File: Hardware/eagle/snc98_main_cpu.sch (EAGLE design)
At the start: 88 parts, among them IC1 MCP170333MB, M1 IRLML2244, M12 IRLML2244, M2 IRLML2244, M3 IRLML2244, T1 BCR135, T2 BCR135, T3 BCR185, U1 74HC4051_MUX, U2 DS18B20, U3 ATMEGA1284P-PU, U4 TLV70033 / TC1185, Y2 12MHz

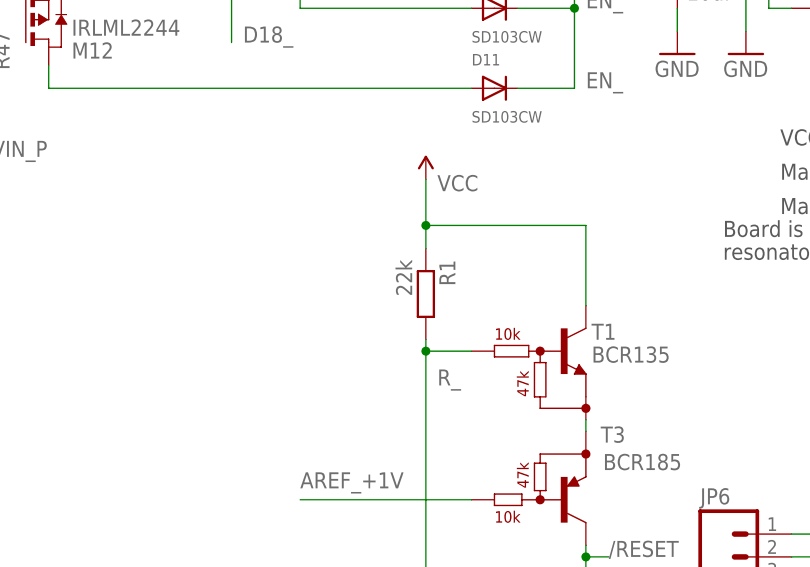
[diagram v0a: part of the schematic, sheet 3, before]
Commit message: Work like WIN_7 Calculator in "Standard Mode"
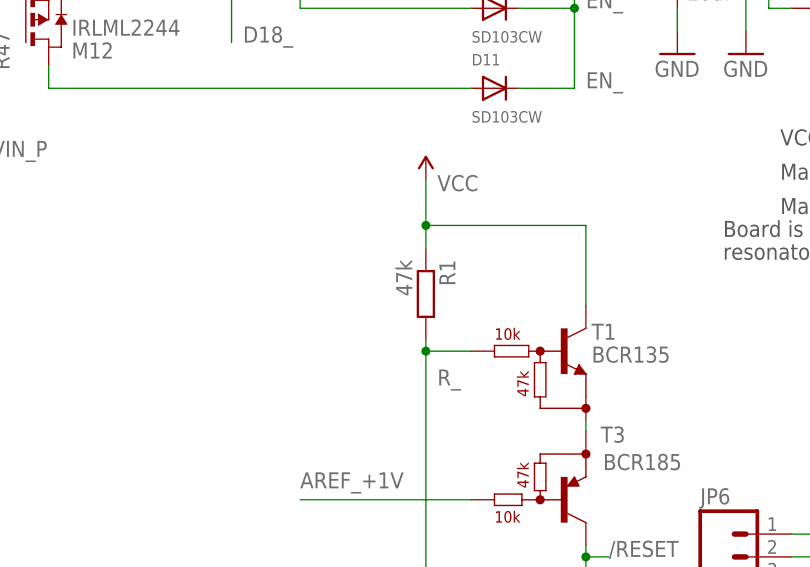
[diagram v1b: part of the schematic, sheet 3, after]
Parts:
- R1: value 22k -> 47k
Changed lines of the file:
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@@
 <setting verticaltext="up"/>
 </settings>
-<grid distance="0.1" unitdist="inch" unit="inch" style="lines" multiple="1" display="yes" altdistance="0.05" altunitdist="inch" altunit="inch"/>
+<grid distance="0.1" unitdist="inch" unit="mil" style="lines" multiple="1" display="no" altdistance="0.05" altunitdist="inch" altunit="inch"/>
 <layers>
 <layer number="1" name="Top" color="4" fill="1" visible="no" active="no"/>
@@
 <part name="U3" library="Atmel_By_element14_Batch_1-00" deviceset="ATMEGA1284P-PU" device=""/>
 <part name="R50" library="rcl" deviceset="R-EU_" device="R1206" value="6k8"/>
-<part name="R1" library="rcl" deviceset="R-EU_" device="R1206" value="22k"/>
+<part name="R1" library="rcl" deviceset="R-EU_" device="R1206" value="47k"/>
 <part name="R4" library="rcl" deviceset="R-EU_" device="R1206" value="100"/>
 <part name="R51" library="rcl" deviceset="R-EU_" device="R1206" value="3k3"/>

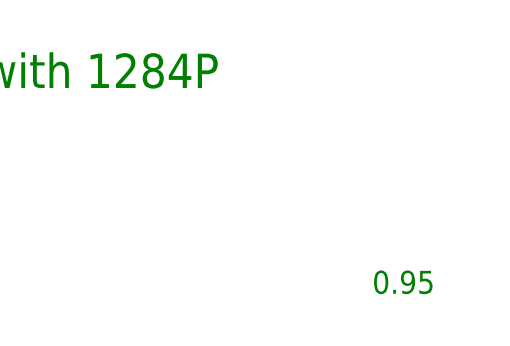
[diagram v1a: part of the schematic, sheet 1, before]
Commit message: Version 4 mechanical change
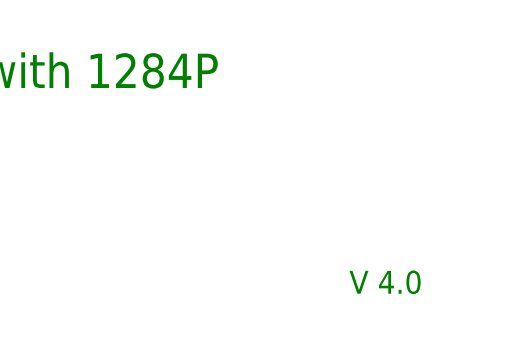
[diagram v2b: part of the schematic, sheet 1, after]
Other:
- note added: "V 4.0"
- note removed: "0.95"
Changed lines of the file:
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@@
 <setting verticaltext="up"/>
 </settings>
-<grid distance="0.1" unitdist="inch" unit="mil" style="lines" multiple="1" display="no" altdistance="0.05" altunitdist="inch" altunit="inch"/>
+<grid distance="0.1" unitdist="inch" unit="inch" style="lines" multiple="1" display="yes" altdistance="0.05" altunitdist="inch" altunit="inch"/>
 <layers>
 <layer number="1" name="Top" color="4" fill="1" visible="no" active="no"/>
@@
 <text x="149.86" y="30.48" size="3.81" layer="91" ratio="12">Calculator 15-Digit with 1284P</text>
 <text x="149.86" y="25.4" size="2.54" layer="91" ratio="12">by Jens Grabner</text>
-<text x="238.76" y="7.62" size="2.54" layer="91" ratio="12">0.95</text>
+<text x="236.22" y="7.62" size="2.54" layer="91" ratio="12">V 4.0</text>
 <text x="5.08" y="10.16" size="2.1844" layer="91" ratio="10">Calculator 15-Digit with ATmega1284P by Jens Grabner is licensed under</text>
 <text x="5.08" y="15.24" size="3.81" layer="91" ratio="12">Copyright CERN 2013</text>
@@
 <text x="149.86" y="30.48" size="3.81" layer="91" ratio="12">Calculator 15-Digit with 1284P</text>
 <text x="149.86" y="25.4" size="2.54" layer="91" ratio="12">by Jens Grabner</text>
-<text x="238.76" y="7.62" size="2.54" layer="91" ratio="12">0.95</text>
+<text x="236.22" y="7.62" size="2.54" layer="91" ratio="12">V 4.0</text>
 <text x="5.08" y="10.16" size="2.1844" layer="91" ratio="10">Calculator 15-Digit with ATmega1284P by Jens Grabner is licensed under</text>
 <text x="5.08" y="15.24" size="3.81" layer="91" ratio="12">Copyright CERN 2013</text>
@@
 <text x="149.86" y="30.48" size="3.81" layer="91" ratio="12">Calculator 15-Digit with 1284P</text>
 <text x="149.86" y="25.4" size="2.54" layer="91" ratio="12">by Jens Grabner</text>
-<text x="238.76" y="7.62" size="2.54" layer="91" ratio="12">0.95</text>
+<text x="236.22" y="7.62" size="2.54" layer="91" ratio="12">V 4.0</text>
 <text x="5.08" y="10.16" size="2.1844" layer="91" ratio="10">Calculator 15-Digit with ATmega1284P by Jens Grabner is licensed under</text>
 <text x="5.08" y="15.24" size="3.81" layer="91" ratio="12">Copyright CERN 2013</text>

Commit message: V 5.0 Hardware - Design
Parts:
- removed JP5: ICSP, _jc:AVR_SPI_PRG_62X3_LOCK
- added JP1: ICSP, _jc:AVR_SPI_PRG_6
- C12: value 47n -> 220n
- C2: value 100nF -> 220nF
- C20, C21: value 10uF -> 4.7uF
- C7, C8: value 22pF -> 15pF
- R25: value 1k -> 100
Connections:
- net /RESET: now also JP1.RST; no longer JP5.RST
- net D5_: now also JP1.MOSI; no longer JP5.MOSI
- net D6_: now also JP1.MISO; no longer JP5.MISO
- net D7_: now also JP1.SCK; no longer JP5.SCK
- net GND-ISO: now also JP1.GND; no longer JP5.GND
- net VCC: now also JP1.VCC; no longer JP5.VCC
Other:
- note added: "V 5.0"
- note removed: "V 4.0"

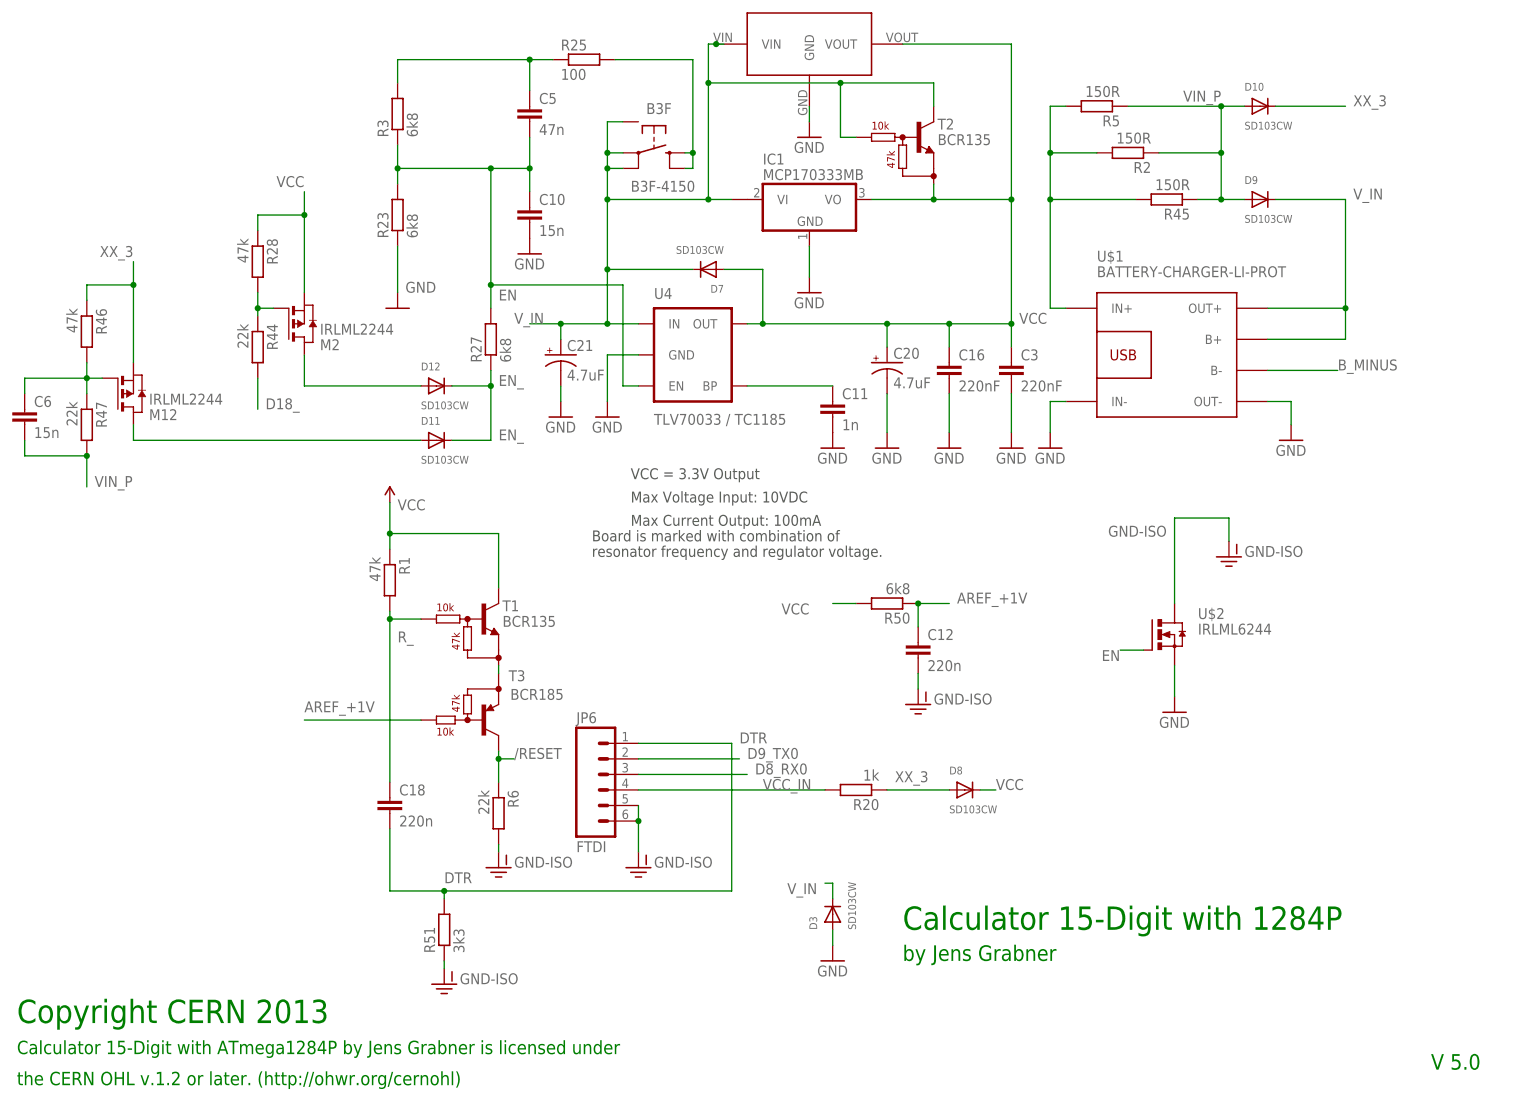
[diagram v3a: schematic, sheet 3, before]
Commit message: PCB cleaning V1.1
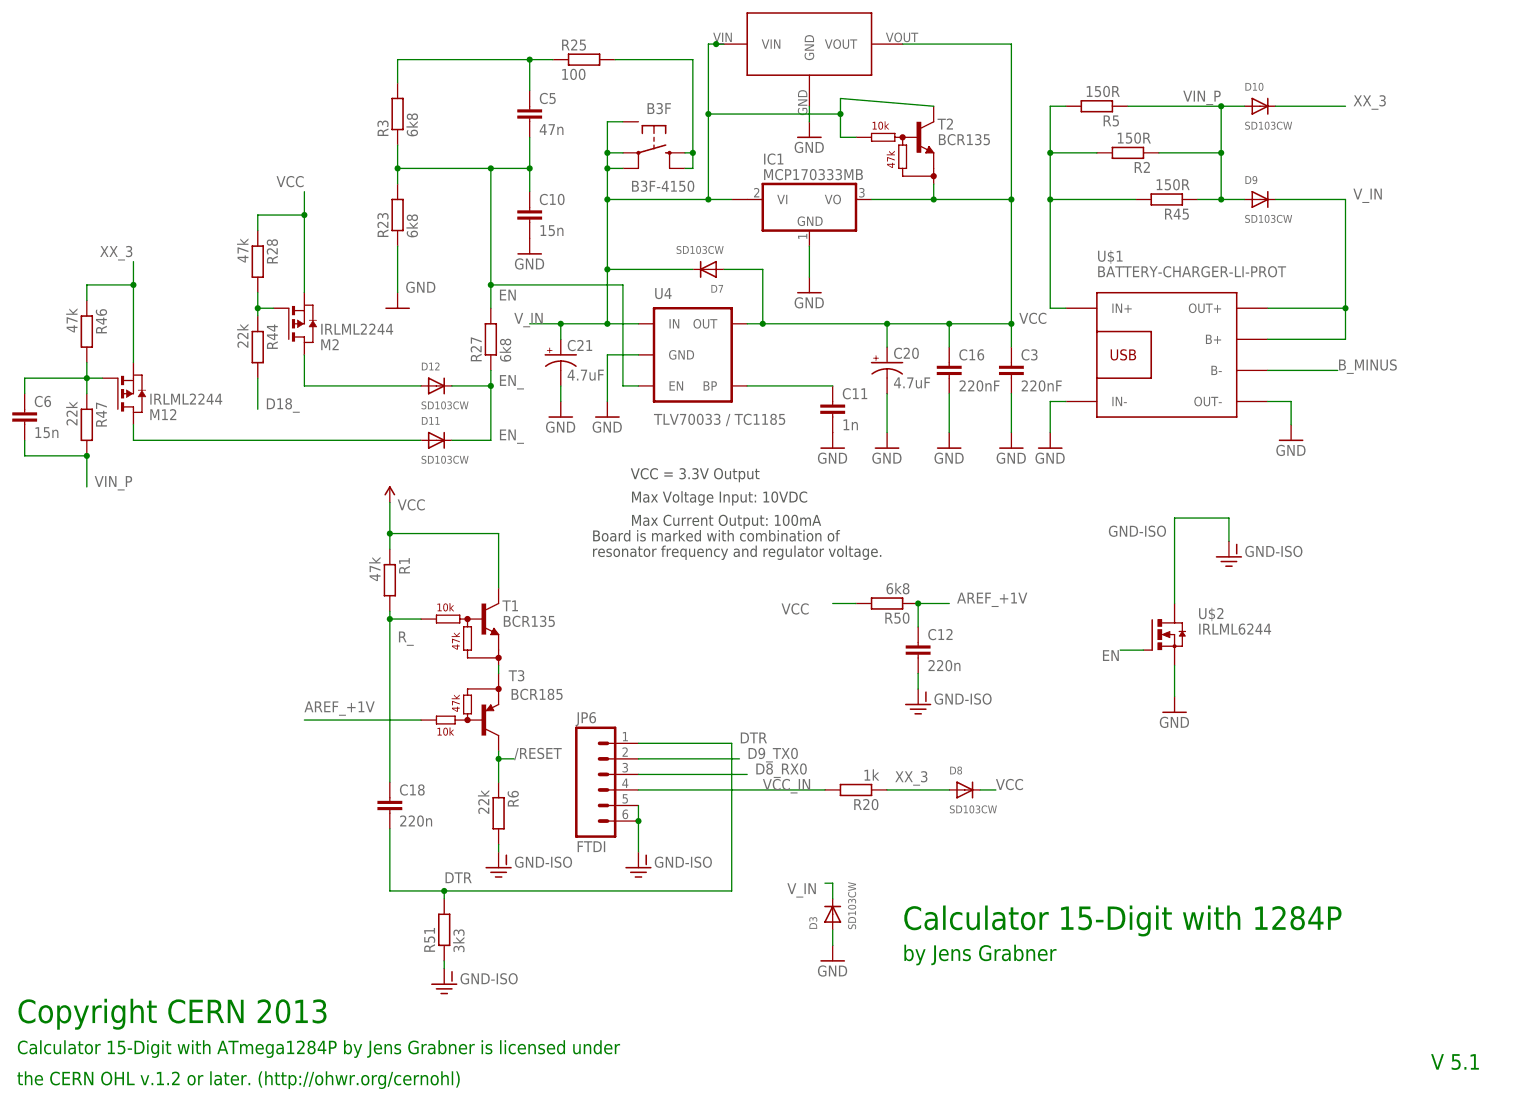
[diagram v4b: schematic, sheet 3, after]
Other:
- note added: "V 5.1"
- note removed: "V 5.0"
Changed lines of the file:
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@@
 <text x="149.86" y="30.48" size="3.81" layer="91" ratio="12">Calculator 15-Digit with 1284P</text>
 <text x="149.86" y="25.4" size="2.54" layer="91" ratio="12">by Jens Grabner</text>
-<text x="236.22" y="7.62" size="2.54" layer="91" ratio="12">V 5.0</text>
+<text x="236.22" y="7.62" size="2.54" layer="91" ratio="12">V 5.1</text>
 <text x="5.08" y="10.16" size="2.1844" layer="91" ratio="10">Calculator 15-Digit with ATmega1284P by Jens Grabner is licensed under</text>
 <text x="5.08" y="15.24" size="3.81" layer="91" ratio="12">Copyright CERN 2013</text>
@@
 <text x="149.86" y="30.48" size="3.81" layer="91" ratio="12">Calculator 15-Digit with 1284P</text>
 <text x="149.86" y="25.4" size="2.54" layer="91" ratio="12">by Jens Grabner</text>
-<text x="236.22" y="7.62" size="2.54" layer="91" ratio="12">V 5.0</text>
+<text x="236.22" y="7.62" size="2.54" layer="91" ratio="12">V 5.1</text>
 <text x="5.08" y="10.16" size="2.1844" layer="91" ratio="10">Calculator 15-Digit with ATmega1284P by Jens Grabner is licensed under</text>
 <text x="5.08" y="15.24" size="3.81" layer="91" ratio="12">Copyright CERN 2013</text>
@@
 <text x="149.86" y="30.48" size="3.81" layer="91" ratio="12">Calculator 15-Digit with 1284P</text>
 <text x="149.86" y="25.4" size="2.54" layer="91" ratio="12">by Jens Grabner</text>
-<text x="236.22" y="7.62" size="2.54" layer="91" ratio="12">V 5.0</text>
+<text x="236.22" y="7.62" size="2.54" layer="91" ratio="12">V 5.1</text>
 <text x="5.08" y="10.16" size="2.1844" layer="91" ratio="10">Calculator 15-Digit with ATmega1284P by Jens Grabner is licensed under</text>
 <text x="5.08" y="15.24" size="3.81" layer="91" ratio="12">Copyright CERN 2013</text>
@@
 <wire x1="120.65" y1="175.26" x2="119.38" y2="175.26" width="0.1524" layer="91"/>
 <wire x1="119.38" y1="175.26" x2="118.11" y2="175.26" width="0.1524" layer="91"/>
-<wire x1="118.11" y1="175.26" x2="118.11" y2="168.91" width="0.1524" layer="91"/>
+<wire x1="118.11" y1="175.26" x2="118.11" y2="163.83" width="0.1524" layer="91"/>
 <junction x="118.11" y="149.86"/>
 <pinref part="U$3" gate="G$1" pin="VIN"/>
 <junction x="119.38" y="175.26"/>
 <pinref part="S3" gate="S" pin="5"/>
-<wire x1="118.11" y1="168.91" x2="118.11" y2="149.86" width="0.1524" layer="91"/>
+<wire x1="118.11" y1="163.83" x2="118.11" y2="149.86" width="0.1524" layer="91"/>
 <wire x1="104.14" y1="162.56" x2="101.6" y2="162.56" width="0.1524" layer="91"/>
 <wire x1="101.6" y1="162.56" x2="101.6" y2="157.48" width="0.1524" layer="91"/>
 <junction x="101.6" y="157.48"/>
 <pinref part="T2" gate="T$1" pin="C"/>
-<wire x1="154.94" y1="165.1" x2="154.94" y2="168.91" width="0.1524" layer="91"/>
-<wire x1="154.94" y1="168.91" x2="139.7" y2="168.91" width="0.1524" layer="91"/>
-<junction x="118.11" y="168.91"/>
+<wire x1="154.94" y1="165.1" x2="139.7" y2="166.37" width="0.1524" layer="91"/>
+<wire x1="139.7" y1="166.37" x2="139.7" y2="163.83" width="0.1524" layer="91"/>
+<junction x="118.11" y="163.83"/>
 <pinref part="T2" gate="T$1" pin="B"/>
-<wire x1="139.7" y1="168.91" x2="118.11" y2="168.91" width="0.1524" layer="91"/>
+<wire x1="139.7" y1="163.83" x2="118.11" y2="163.83" width="0.1524" layer="91"/>
 <wire x1="142.24" y1="160.02" x2="139.7" y2="160.02" width="0.1524" layer="91"/>
-<wire x1="139.7" y1="160.02" x2="139.7" y2="168.91" width="0.1524" layer="91"/>
-<junction x="139.7" y="168.91"/>
-</segment>
-<segment>
+<wire x1="139.7" y1="160.02" x2="139.7" y2="163.83" width="0.1524" layer="91"/>
+<junction x="139.7" y="163.83"/>
+</segment>
+<segment>

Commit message: sinh()_cosh()_tanh() added
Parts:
- BH10, BH11, BH12, BH7, BH8, BH9, C1, C10, C11, C12, C13, C14, C15, C16, C18, C2, C20, C21, C22, C3, C4, C5, C6, C7, C8, C9, IC1, JP1, JP13, JP14, JP15, JP3, JP6, LOGO1, R1, R2, R20, R21, R22, R23, R25, R27, R28, R3, R31, R32, R33, R34, R35, R4, R44, R45, R46, R47, R48, R5, R50, R51, R6, R7, SG1, U$1, U$3, U1, U2, U4, Y2: OC_FARNELL (none) -> unknown
- D1, D10, D11, D12, D2, D3, D4, D5, D7, D8, D9: MF (none) -> MULTICOMP; MPN (none) -> SD103CW-7-F; OC_FARNELL (none) -> 2306221
- M1, M12, M2, M3: MF (none) -> INFINEON; MPN (none) -> IRLML2244TRPBF; OC_FARNELL (none) -> 2468051
- S3: MF (none) -> OMRON; MPN (none) -> B3F4150; OC_FARNELL (none) -> 1960976
- T1, T2: MF (none) -> INFINEON; MPN (none) -> BCR135E6327HTSA1; OC_FARNELL (none) -> 2443491RL
- T3: MF (none) -> ROHM; MPN (none) -> DTA114YKAT146; OC_FARNELL (none) -> 1680186
- U$2: MF (none) -> INFINEON; MPN (none) -> IRLML6244TRPBF; OC_FARNELL (none) -> 1864517
- U3: MF (none) -> MICROCHIP
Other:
- note added: "V 1.1"
- note removed: "V 5.1"
- moved on the sheet: T2
